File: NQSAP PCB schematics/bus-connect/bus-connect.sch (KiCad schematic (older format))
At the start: 18 parts, among them J1 Bus, J2 Bus

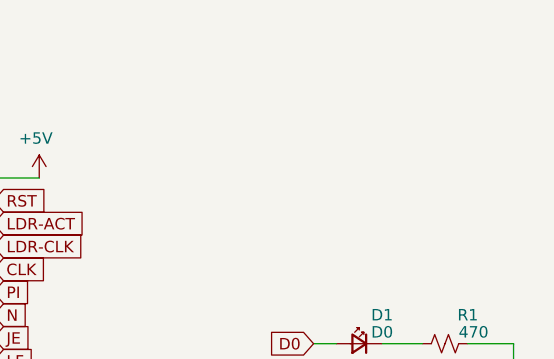
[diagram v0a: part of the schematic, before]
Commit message: Add RAM, update and add gerbers for new boards
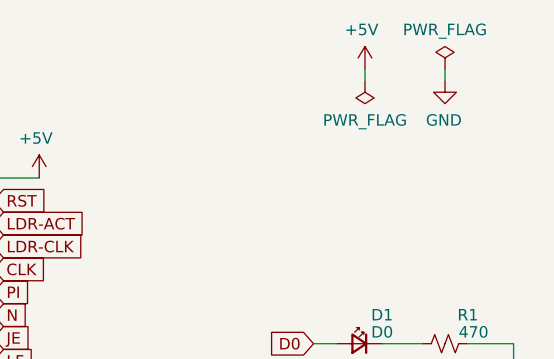
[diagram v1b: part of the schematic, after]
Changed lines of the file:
@@
 encoding utf-8
 Sheet 1 1
-Title "NQSAP Bus Connector"
-Date "2021-10-03"
-Rev "1.0"
+Title "NQSAP-PCB Bus Connector"
+Date "2021-10-24"
+Rev "1.1"
 Comp "github.com/TomNisbet/nqsap-pcb"
 Comment1 ""
@@
 Wire Wire Line
 	7350 4200 7350 4275
+$Comp
+L power:PWR_FLAG #FLG0101
+U 1 1 621002EB
+P 7050 1250
+F 0 "#FLG0101" H 7050 1325 50  0001 C CNN
+F 1 "PWR_FLAG" H 7050 1423 50  0000 C CNN
+F 2 "" H 7050 1250 50  0001 C CNN
+F 3 "~" H 7050 1250 50  0001 C CNN
+	1    7050 1250
+	1    0    0    -1
+$EndComp
+$Comp
+L power:PWR_FLAG #FLG0102
+U 1 1 6210088A
+P 6700 1300
+F 0 "#FLG0102" H 6700 1375 50  0001 C CNN
+F 1 "PWR_FLAG" H 6700 1473 50  0000 C CNN
+F 2 "" H 6700 1300 50  0001 C CNN
+F 3 "~" H 6700 1300 50  0001 C CNN
+	1    6700 1300
+	1    0    0    1
+$EndComp
+$Comp
+L power:+5V #PWR0101
+U 1 1 62100F53
+P 6700 1250
+F 0 "#PWR0101" H 6700 1100 50  0001 C CNN
+F 1 "+5V" H 6715 1423 50  0000 C CNN
+F 2 "" H 6700 1250 50  0001 C CNN
+F 3 "" H 6700 1250 50  0001 C CNN
+	1    6700 1250
+	-1   0    0    -1
+$EndComp
+$Comp
+L power:GND #PWR0102
+U 1 1 6210188D
+P 7050 1300
+F 0 "#PWR0102" H 7050 1050 50  0001 C CNN
+F 1 "GND" H 7055 1127 50  0000 C CNN
+F 2 "" H 7050 1300 50  0001 C CNN
+F 3 "" H 7050 1300 50  0001 C CNN
+	1    7050 1300
+	-1   0    0    -1
+$EndComp
+Wire Wire Line
+	7050 1250 7050 1300
+Wire Wire Line
+	6700 1250 6700 1300
 $EndSCHEMATC

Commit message: KiCad schematics, PCBs, and gerbers for the ALU and flags modules
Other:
- note added: "The resistor and LED pairs can also be populated to create\na bus termination board. Use a 1K resistor for the R values\nand a 0 Ohm for the D values to get a 1K bus termination.\nOr use pairs of 470 Ohm resistors for a 940 Ohm termination."
- moved on the sheet: D1, D2, D3, D4, D5, D6, D7, D8, R1, R2, R3, R4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
